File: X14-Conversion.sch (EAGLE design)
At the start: 23 parts, among them P1 282837-2, P2 282837-2, P3 282837-2, U2 LM2678SD-ADJ/NOPB

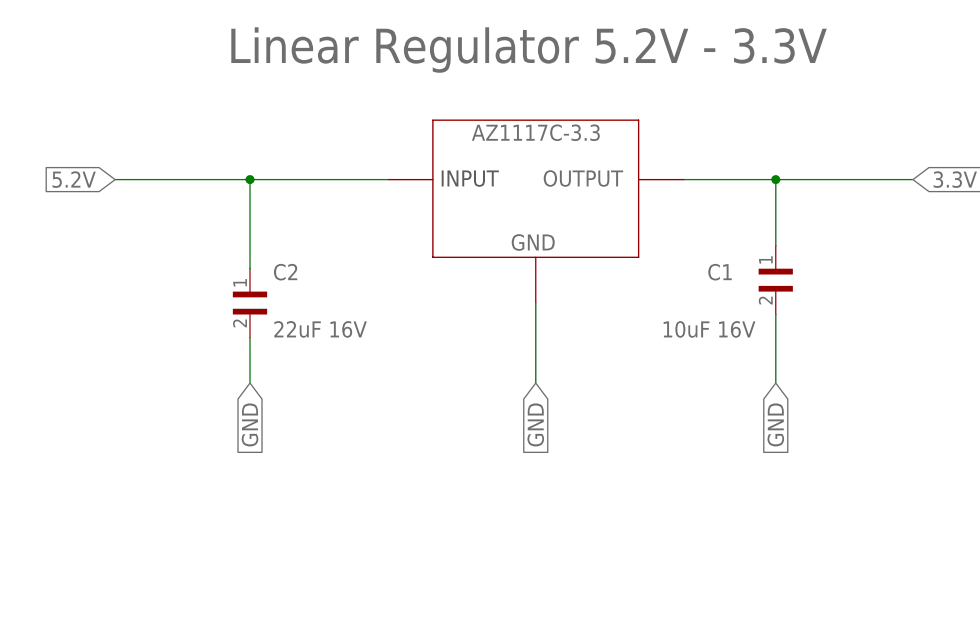
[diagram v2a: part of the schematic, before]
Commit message: Fix capacitors on Linear Regulator
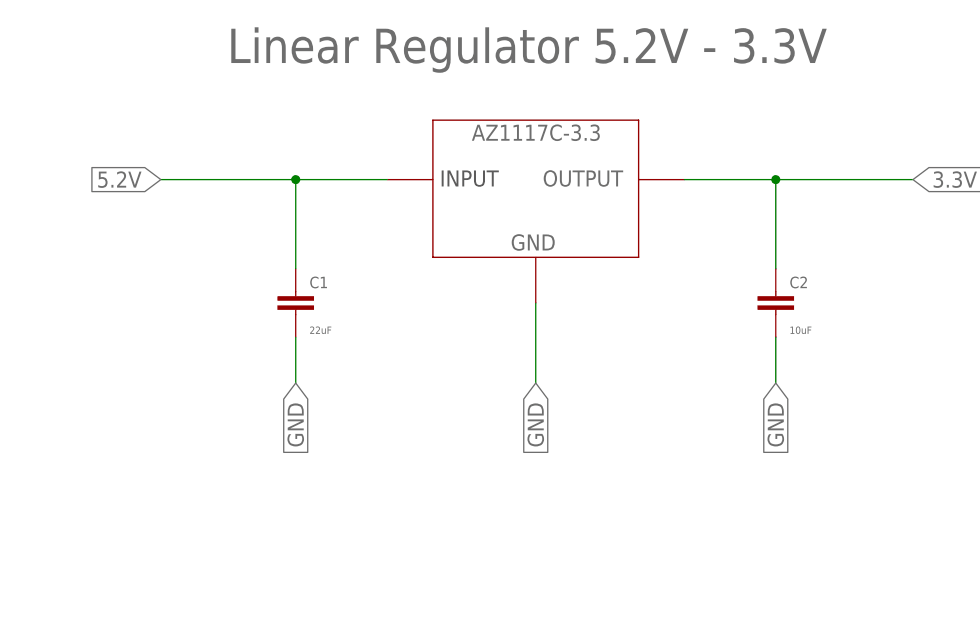
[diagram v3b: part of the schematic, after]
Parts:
- AZ1117C: value SOT150P410X160-3N -> AZ1117C-3.3
- C1: value 10uF 16V -> 22uF; device CAP_GRM21BR61C106KE15L:GRM21BR61C106KE15L -> SparkFun-Capacitors:22UF-0805-6.3V-20%
- C2: value 22uF 16V -> 10uF; device CAP_GRM21BR61C226ME44L:GRM21BR61C226ME44L -> SparkFun-Capacitors:10UF-0603-6.3V-20%
- renumbered U$1 to AZ1117C, U2 to LM2678
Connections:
- net 3.3V: now also C2.1; no longer C1.1
- net 5.2V: now also C1.1; no longer C2.1
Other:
- moved on the sheet: C1, C2
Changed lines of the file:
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@@
 <part name="COUT" library="16SVP180MX" deviceset="16SVP180MX" device="" value="180uF 30mΩ"/>
 <part name="FRAME1" library="frames" library_urn="urn:adsk.eagle:library:229" deviceset="A3L-LOC" device=""/>
-<part name="U$1" library="AZ1117C-3.3" deviceset="SOT150P410X160-3N" device=""/>
-<part name="C1" library="CAP_GRM21BR61C106KE15L" deviceset="GRM21BR61C106KE15L" device="" value="10uF 16V"/>
-<part name="C2" library="CAP_GRM21BR61C226ME44L" deviceset="GRM21BR61C226ME44L" device="" value="22uF 16V"/>
+<part name="AZ1117C" library="AZ1117C-3.3" deviceset="SOT150P410X160-3N" device="" value="AZ1117C-3.3"/>
 <part name="CONN" library="CONN, Distribution-Conversion" deviceset="DISTRIBUTION-CONVERSION" device=""/>
-<part name="U2" library="LM2678SX-ADJNOPB" deviceset="LM2678SD-ADJ/NOPB" device=""/>
+<part name="LM2678" library="LM2678SX-ADJNOPB" deviceset="LM2678SD-ADJ/NOPB" device=""/>
 <part name="U$2" library="testpoints" deviceset="3.3V_TESTPOINT" device=""/>
 <part name="U$3" library="testpoints" deviceset="5.2V_TESTPOINT" device=""/>
@@
 <part name="CB" library="SparkFun-Capacitors" library_urn="urn:adsk.eagle:library:510" deviceset="10NF" device="-0603-50V-10%" package3d_urn="urn:adsk.eagle:package:37414/1" value="10nF 0Ω"/>
 <part name="CINX" library="SparkFun-Capacitors" library_urn="urn:adsk.eagle:library:510" deviceset="0.1UF" device="-0603-25V-(+80/-20%)" package3d_urn="urn:adsk.eagle:package:37414/1" value="0.1uF 1mΩ"/>
+<part name="C2" library="SparkFun-Capacitors" library_urn="urn:adsk.eagle:library:510" deviceset="10UF" device="-0603-6.3V-20%" package3d_urn="urn:adsk.eagle:package:37414/1" value="10uF"/>
+<part name="C1" library="SparkFun-Capacitors" library_urn="urn:adsk.eagle:library:510" deviceset="22UF" device="-0805-6.3V-20%" package3d_urn="urn:adsk.eagle:package:37429/1" value="22uF"/>
 </parts>
 <sheets>
@@
 <attribute name="SHEET" x="179.705" y="-111.76" size="2.54" layer="94"/>
 </instance>
-<instance part="U$1" gate="G$1" x="-75.692" y="-10.668" smashed="yes"/>
-<instance part="C1" gate="G$1" x="-48.26" y="-20.32" smashed="yes" rot="R270">
-<attribute name="NAME" x="-55.88" y="-21.58906875" size="1.77843125" layer="95"/>
-<attribute name="VALUE" x="-60.96" y="-27.94848125" size="1.78096875" layer="96"/>
-</instance>
-<instance part="C2" gate="G$1" x="-106.68" y="-22.86" smashed="yes" rot="R270">
-<attribute name="NAME" x="-104.14" y="-21.58906875" size="1.77843125" layer="95"/>
-<attribute name="VALUE" x="-104.14" y="-27.94848125" size="1.78096875" layer="96"/>
-</instance>
+<instance part="AZ1117C" gate="G$1" x="-75.692" y="-10.668" smashed="yes"/>
 <instance part="CONN" gate="G$1" x="-81.28" y="-83.82" smashed="yes">
 <attribute name="NAME" x="-88.9" y="-76.2" size="1.778" layer="95"/>
 </instance>
-<instance part="U2" gate="A" x="-2.54" y="66.04" smashed="yes">
+<instance part="LM2678" gate="A" x="-2.54" y="66.04" smashed="yes">
 <attribute name="NAME" x="-13.6144" y="79.9846" size="2.0828" layer="95" ratio="6" rot="SR0" display="off"/>
 <attribute name="VALUE" x="-13.4874" y="77.4446" size="2.0828" layer="96" ratio="6" rot="SR0"/>
@@
 <attribute name="VALUE" x="-44.45" y="54.737" size="0.8128" layer="96"/>
 </instance>
+<instance part="C2" gate="G$1" x="-48.26" y="-25.4" smashed="yes">
+<attribute name="NAME" x="-46.736" y="-22.479" size="1.27" layer="95"/>
+<attribute name="VALUE" x="-46.736" y="-27.559" size="0.8128" layer="96"/>
+</instance>
+<instance part="C1" gate="G$1" x="-101.6" y="-25.4" smashed="yes">
+<attribute name="NAME" x="-100.076" y="-22.479" size="1.27" layer="95"/>
+<attribute name="VALUE" x="-100.076" y="-27.559" size="0.8128" layer="96"/>
+</instance>
 </instances>
 <busses>
@@
 <net name="GND" class="0">
 <segment>
-<pinref part="C2" gate="G$1" pin="2"/>
-<wire x1="-106.68" y1="-27.94" x2="-106.68" y2="-33.02" width="0.1524" layer="91"/>
-<label x="-106.68" y="-33.02" size="1.778" layer="95" rot="R270" xref="yes"/>
-</segment>
-<segment>
-<pinref part="U$1" gate="G$1" pin="GND"/>
+<wire x1="-101.6" y1="-27.94" x2="-101.6" y2="-33.02" width="0.1524" layer="91"/>
+<label x="-101.6" y="-33.02" size="1.778" layer="95" rot="R270" xref="yes"/>
+<pinref part="C1" gate="G$1" pin="2"/>
+</segment>
+<segment>
+<pinref part="AZ1117C" gate="G$1" pin="GND"/>
 <wire x1="-74.93" y1="-24.13" x2="-74.93" y2="-33.02" width="0.1524" layer="91"/>
 <label x="-74.93" y="-33.02" size="1.778" layer="95" rot="R270" xref="yes"/>
 </segment>
 <segment>
-<pinref part="C1" gate="G$1" pin="2"/>
-<wire x1="-48.26" y1="-33.02" x2="-48.26" y2="-25.4" width="0.1524" layer="91"/>
+<wire x1="-48.26" y1="-33.02" x2="-48.26" y2="-27.94" width="0.1524" layer="91"/>
 <label x="-48.26" y="-33.02" size="1.778" layer="95" rot="R270" xref="yes"/>
+<pinref part="C2" gate="G$1" pin="2"/>
 </segment>
 <segment>
@@
 <wire x1="-45.72" y1="33.02" x2="-27.94" y2="33.02" width="0.1524" layer="91"/>
 <junction x="2.54" y="33.02"/>
-<pinref part="U2" gate="A" pin="GND"/>
+<pinref part="LM2678" gate="A" pin="GND"/>
 <wire x1="-27.94" y1="33.02" x2="2.54" y2="33.02" width="0.1524" layer="91"/>
 <wire x1="-22.098" y1="68.326" x2="-27.94" y2="68.326" width="0.1524" layer="91"/>
 <wire x1="-27.94" y1="68.326" x2="-27.94" y2="65.786" width="0.1524" layer="91"/>
 <junction x="-27.94" y="33.02"/>
-<pinref part="U2" gate="A" pin="DAP"/>
+<pinref part="LM2678" gate="A" pin="DAP"/>
 <wire x1="-27.94" y1="65.786" x2="-27.94" y2="33.02" width="0.1524" layer="91"/>
 <wire x1="-22.098" y1="65.786" x2="-27.94" y2="65.786" width="0.1524" layer="91"/>
@@
 <net name="3.3V" class="0">
 <segment>
-<pinref part="U$1" gate="G$1" pin="OUTPUT"/>
+<pinref part="AZ1117C" gate="G$1" pin="OUTPUT"/>
 <wire x1="-58.42" y1="-10.414" x2="-48.26" y2="-10.414" width="0.1524" layer="91"/>
-<pinref part="C1" gate="G$1" pin="1"/>
 <wire x1="-48.26" y1="-10.414" x2="-33.02" y2="-10.414" width="0.1524" layer="91"/>
-<wire x1="-48.26" y1="-17.78" x2="-48.26" y2="-10.414" width="0.1524" layer="91"/>
+<wire x1="-48.26" y1="-20.32" x2="-48.26" y2="-10.414" width="0.1524" layer="91"/>
 <junction x="-48.26" y="-10.414"/>
 <label x="-33.02" y="-10.414" size="1.778" layer="95" xref="yes"/>
+<pinref part="C2" gate="G$1" pin="1"/>
 </segment>
 <segment>
@@
 <net name="5.2V" class="0">
 <segment>
-<pinref part="U$1" gate="G$1" pin="INPUT"/>
-<wire x1="-121.666" y1="-10.414" x2="-106.68" y2="-10.414" width="0.1524" layer="91"/>
-<pinref part="C2" gate="G$1" pin="1"/>
-<wire x1="-106.68" y1="-10.414" x2="-91.44" y2="-10.414" width="0.1524" layer="91"/>
-<wire x1="-106.68" y1="-20.32" x2="-106.68" y2="-10.414" width="0.1524" layer="91"/>
-<junction x="-106.68" y="-10.414"/>
-<label x="-121.666" y="-10.414" size="1.778" layer="95" rot="R180" xref="yes"/>
+<pinref part="AZ1117C" gate="G$1" pin="INPUT"/>
+<wire x1="-116.586" y1="-10.414" x2="-101.6" y2="-10.414" width="0.1524" layer="91"/>
+<wire x1="-101.6" y1="-10.414" x2="-91.44" y2="-10.414" width="0.1524" layer="91"/>
+<wire x1="-101.6" y1="-20.32" x2="-101.6" y2="-10.414" width="0.1524" layer="91"/>
+<junction x="-101.6" y="-10.414"/>
+<label x="-116.586" y="-10.414" size="1.778" layer="95" rot="R180" xref="yes"/>
+<pinref part="C1" gate="G$1" pin="1"/>
 </segment>
 <segment>
@@
 </segment>
 <segment>
-<pinref part="U2" gate="A" pin="VIN"/>
+<pinref part="LM2678" gate="A" pin="VIN"/>
 <wire x1="-22.098" y1="73.406" x2="-45.72" y2="73.406" width="0.1524" layer="91"/>
 <wire x1="-45.72" y1="73.406" x2="-45.72" y2="60.96" width="0.1524" layer="91"/>
@@
 <net name="N$2" class="0">
 <segment>
-<pinref part="U2" gate="A" pin="SW"/>
+<pinref part="LM2678" gate="A" pin="SW"/>
 <pinref part="L1" gate="G$1" pin="1"/>
 <wire x1="26.162" y1="65.786" x2="37.084" y2="65.786" width="0.1524" layer="91"/>
@@
 <net name="N$4" class="0">
 <segment>
-<pinref part="U2" gate="A" pin="BOOST"/>
+<pinref part="LM2678" gate="A" pin="BOOST"/>
 <wire x1="26.162" y1="68.326" x2="26.162" y2="70.358" width="0.1524" layer="91"/>
 <wire x1="26.162" y1="70.358" x2="29.21" y2="70.358" width="0.1524" layer="91"/>
@@
 <net name="N$5" class="0">
 <segment>
-<pinref part="U2" gate="A" pin="FB"/>
+<pinref part="LM2678" gate="A" pin="FB"/>
 <wire x1="26.162" y1="73.406" x2="30.48" y2="73.406" width="0.1524" layer="91"/>
 <wire x1="30.48" y1="73.406" x2="30.48" y2="78.486" width="0.1524" layer="91"/>

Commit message: Fix Footprints
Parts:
- CIN: device 20SVPF120M:20SVPF120MPCAP_SVP_C6_PAN -> 20SVPF120M:20SVPF120M
- D1: device CDBC520-G_Library:CDBC520-GCDBC-G -> CDBC520-G_Library:CDBG520-G
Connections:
- net 3.3V: now also AZ1117C.VOUT
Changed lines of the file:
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@@
 </classes>
 <parts>
-<part name="D1" library="CDBC520-G_Library" deviceset="CDBC520-G" device="CDBC-G" value="550mV 5A"/>
-<part name="CIN" library="20SVPF120M" deviceset="20SVPF120M" device="PCAP_SVP_C6_PAN" value="120uF 25mΩ"/>
 <part name="L1" library="IND, 15uH - hcma1305" deviceset="HCMA1305" device="" package3d_urn="urn:adsk.eagle:package:24201702/2" value="15uH"/>
 <part name="COUT" library="16SVP180MX" deviceset="16SVP180MX" device="" value="180uF 30mΩ"/>
@@
 <part name="C2" library="SparkFun-Capacitors" library_urn="urn:adsk.eagle:library:510" deviceset="10UF" device="-0603-6.3V-20%" package3d_urn="urn:adsk.eagle:package:37414/1" value="10uF"/>
 <part name="C1" library="SparkFun-Capacitors" library_urn="urn:adsk.eagle:library:510" deviceset="22UF" device="-0805-6.3V-20%" package3d_urn="urn:adsk.eagle:package:37429/1" value="22uF"/>
+<part name="D1" library="CDBC520-G_Library" deviceset="CDBG520-G" device="" value="550mV 5A"/>
+<part name="CIN" library="20SVPF120M" deviceset="20SVPF120M" device="" value="120uF 25mΩ"/>
 </parts>
 <sheets>
@@
 </plain>
 <instances>
-<instance part="D1" gate="A" x="37.084" y="54.356" smashed="yes" rot="R270">
-<attribute name="VALUE" x="40.5669" y="48.1711" size="0.8128" layer="96" ratio="10"/>
-<attribute name="NAME" x="40.6192" y="49.5681" size="1.27" layer="95" ratio="10"/>
-</instance>
-<instance part="CIN" gate="A" x="-66.04" y="60.96" smashed="yes" rot="R270">
-<attribute name="VALUE" x="-62.5571" y="55.6641" size="0.8128" layer="96" ratio="10"/>
-<attribute name="NAME" x="-62.5048" y="57.9501" size="1.27" layer="95" ratio="10"/>
-</instance>
 <instance part="L1" gate="G$1" x="46.99" y="65.786" smashed="yes">
 <attribute name="NAME" x="53.34" y="67.564" size="1.27" layer="95"/>
@@
 <attribute name="VALUE" x="-100.076" y="-27.559" size="0.8128" layer="96"/>
 </instance>
+<instance part="D1" gate="A" x="37.084" y="54.356" smashed="yes" rot="R270">
+<attribute name="VALUE" x="40.8209" y="48.1711" size="0.8128" layer="96" ratio="10"/>
+<attribute name="NAME" x="40.8732" y="49.8221" size="1.27" layer="95" ratio="10"/>
+</instance>
+<instance part="CIN" gate="G$1" x="-66.04" y="60.96" smashed="yes" rot="R270">
+<attribute name="VALUE" x="-62.5571" y="56.1721" size="0.8128" layer="96" ratio="10"/>
+<attribute name="NAME" x="-62.5048" y="57.9501" size="1.27" layer="95" ratio="10"/>
+</instance>
 </instances>
 <busses>
@@
 <wire x1="2.54" y1="33.02" x2="2.54" y2="27.94" width="0.1524" layer="91"/>
 <label x="2.54" y="27.94" size="1.778" layer="95" rot="R270" xref="yes"/>
-<pinref part="D1" gate="A" pin="2"/>
 <wire x1="37.084" y1="44.196" x2="37.084" y2="33.02" width="0.1524" layer="91"/>
 <junction x="37.084" y="33.02"/>
@@
 <wire x1="-22.098" y1="65.786" x2="-27.94" y2="65.786" width="0.1524" layer="91"/>
 <junction x="-27.94" y="65.786"/>
-<pinref part="CIN" gate="A" pin="2"/>
 <wire x1="-45.72" y1="33.02" x2="-66.04" y2="33.02" width="0.1524" layer="91"/>
 <wire x1="-66.04" y1="33.02" x2="-66.04" y2="53.34" width="0.1524" layer="91"/>
@@
 <junction x="66.294" y="33.02"/>
 <pinref part="CINX" gate="G$1" pin="2"/>
+<pinref part="D1" gate="A" pin="2"/>
+<pinref part="CIN" gate="G$1" pin="2"/>
 </segment>
 <segment>
@@
 <pinref part="P3" gate="G$1" pin="2"/>
 <wire x1="99.06" y1="-22.86" x2="99.06" y2="-20.32" width="0.1524" layer="91"/>
-<wire x1="99.06" y1="-20.32" x2="111.76" y2="-20.32" width="0.1524" layer="91"/>
-<label x="111.76" y="-20.32" size="1.778" layer="95" xref="yes"/>
 </segment>
 <segment>
@@
 <wire x1="99.06" y1="-27.94" x2="111.76" y2="-27.94" width="0.1524" layer="91"/>
 <label x="111.76" y="-27.94" size="1.778" layer="95" xref="yes"/>
+</segment>
+<segment>
+<wire x1="99.06" y1="-2.54" x2="111.76" y2="-2.54" width="0.1524" layer="91"/>
+<label x="111.76" y="-2.54" size="1.778" layer="95" xref="yes"/>
 </segment>
 </net>
@@
 <label x="-33.02" y="-10.414" size="1.778" layer="95" xref="yes"/>
 <pinref part="C2" gate="G$1" pin="1"/>
+<pinref part="AZ1117C" gate="G$1" pin="VOUT"/>
+<wire x1="-58.42" y1="-6.604" x2="-48.26" y2="-6.604" width="0.1524" layer="91"/>
+<wire x1="-48.26" y1="-6.604" x2="-48.26" y2="-10.414" width="0.1524" layer="91"/>
 </segment>
 <segment>
@@
 <pinref part="P1" gate="G$1" pin="1"/>
 <wire x1="99.06" y1="0" x2="99.06" y2="-2.54" width="0.1524" layer="91"/>
-<wire x1="99.06" y1="-2.54" x2="111.76" y2="-2.54" width="0.1524" layer="91"/>
-<label x="111.76" y="-2.54" size="1.778" layer="95" xref="yes"/>
+</segment>
+<segment>
+<wire x1="99.06" y1="-7.62" x2="111.76" y2="-7.62" width="0.1524" layer="91"/>
+<label x="111.76" y="-7.62" size="1.778" layer="95" xref="yes"/>
 </segment>
 </net>
@@
 <wire x1="-22.098" y1="73.406" x2="-45.72" y2="73.406" width="0.1524" layer="91"/>
 <wire x1="-45.72" y1="73.406" x2="-45.72" y2="60.96" width="0.1524" layer="91"/>
-<pinref part="CIN" gate="A" pin="1"/>
 <wire x1="-66.04" y1="60.96" x2="-66.04" y2="73.406" width="0.1524" layer="91"/>
 <wire x1="-66.04" y1="73.406" x2="-45.72" y2="73.406" width="0.1524" layer="91"/>
@@
 <label x="-75.692" y="73.406" size="1.778" layer="95" rot="R180" xref="yes"/>
 <pinref part="CINX" gate="G$1" pin="1"/>
+<pinref part="CIN" gate="G$1" pin="1"/>
 </segment>
 <segment>
@@
 <pinref part="P2" gate="G$1" pin="2"/>
 <wire x1="99.06" y1="-10.16" x2="99.06" y2="-7.62" width="0.1524" layer="91"/>
-<wire x1="99.06" y1="-7.62" x2="111.76" y2="-7.62" width="0.1524" layer="91"/>
-<label x="111.76" y="-7.62" size="1.778" layer="95" xref="yes"/>
+</segment>
+<segment>
+<wire x1="99.06" y1="-20.32" x2="111.76" y2="-20.32" width="0.1524" layer="91"/>
+<label x="111.76" y="-20.32" size="1.778" layer="95" xref="yes"/>
 </segment>
 </net>
@@
 <wire x1="42.926" y1="70.358" x2="42.926" y2="65.786" width="0.1524" layer="91"/>
 <junction x="42.926" y="65.786"/>
-<pinref part="D1" gate="A" pin="1"/>
 <wire x1="37.084" y1="54.356" x2="37.084" y2="65.786" width="0.1524" layer="91"/>
 <junction x="37.084" y="65.786"/>
 <pinref part="CB" gate="G$1" pin="2"/>
-</segment>
-</net>
+<pinref part="D1" gate="A" pin="1"/>
+</segment>
+</net>
